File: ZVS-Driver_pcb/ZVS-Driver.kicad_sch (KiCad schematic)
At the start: 29 parts, among them J1 Screw_Terminal_01x02, Q1 IRF540N, Q2 IRF540N, Q3 IRF540N, Q4 IRF540N, Q5 IRF540N, U1 LM317_TO-220

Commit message: new after presntation 15/3
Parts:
- removed C3, C4, C5, C6: C, symbol Device:C
- removed D2: D_Schottky, symbol Device:D_Schottky
- removed D5: D_Zener, symbol Device:D_Zener
- removed L4: L, symbol Device:L
- removed R7, R8: R, Resistor_THT:R_Axial_DIN0207_L6.3mm_D2.5mm_P7.62mm_Horizontal, symbol Device:R
- removed U1: LM317_TO-220, Package_TO_SOT_THT:TO-220-3_Vertical, symbol Regulator_Linear:LM317_TO-220
- added D2: D_Zener, Diode_THT:D_DO-41_SOD81_P12.70mm_Horizontal, symbol Device:D_Zener
- added D6: D_Schottky, Diode_THT:D_DO-41_SOD81_P12.70mm_Horizontal, symbol Device:D_Schottky
- added L2: L, Capacitor_THT:CP_Radial_D10.0mm_P5.00mm, symbol Device:L
- C1: footprint (none) -> Library:C_Rect_L7.2mm_W11.0mm_P5.00mm_FKS2_FKP2_MKS2_MKP2
- C2: footprint (none) -> Library:C_Radial_D10.0mm_H20.0mm_P4.5mm,customia
- D1, D3: footprint (none) -> Diode_THT:D_DO-41_SOD81_P12.70mm_Horizontal
- D4: footprint Diode_SMD:D_SOD-523 -> Diode_THT:D_DO-41_SOD81_P12.70mm_Horizontal
- J1: footprint (none) -> Connector_USB:USB_C_Receptacle_GCT_USB4125-xx-x-0190_6P_TopMnt_Horizontal
- L1: footprint (none) -> customia_LC_tank:C_Rect_L7.2mm_W11.0mm_P5.00mm_FKS2_FKP2_MKS2_MKP2
- L3: footprint (none) -> Capacitor_THT:CP_Radial_D10.0mm_P5.00mm
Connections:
- net GND is gone; now on net 0: J1.1 (Pin_1)
- net 0: now also D2.2 (A)
- net at C1.2, L1.2, L3.2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: now also D6.1 (K)
- net at D4.1 (K), R1.1, R3.1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: now also J1.2 (Pin_2), D6.2 (A), L2.1
- net at C1.1, D1.1 (K), L1.1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: now also L2.2
- net at D1.2 (A), Q2.1 (G), Q5.2 (D)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: now also D2.1 (K)
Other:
- moved on the sheet: J1

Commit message: Allages nikou
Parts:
- L2, L3: footprint Capacitor_THT:CP_Radial_D10.0mm_P5.00mm -> Inductor_THT:L_Radial_D10.0mm_P5.00mm_Fastron_07M
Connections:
- net at D4.1 (K), J1.2 (Pin_2), L2.1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: now also L3.1; no longer D6.2 (A)
- net at D3.1 (K), Q1.1 (G), Q4.2 (D)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: now also D6.2 (A); no longer L3.1
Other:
- moved on the sheet: D6, L3
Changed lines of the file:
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@@
+	(wire
+		(pts
+			(xy 241.3 71.12) (xy 242.57 71.12)
+		)
+		(stroke
+			(width 0)
+			(type default)
+		)
+	)
 	(wire
 		(pts
@@
 	(wire
 		(pts
+			(xy 242.57 81.28) (xy 242.57 71.12)
+		)
+		(stroke
+			(width 0)
+			(type default)
+		)
+	)
+	(wire
+		(pts
 			(xy 215.9 91.44) (xy 213.36 91.44)
 		)
@@
 	(wire
 		(pts
+			(xy 214.63 99.06) (xy 217.17 99.06)
+		)
+		(stroke
+			(width 0.1524)
+			(type solid)
+		)
+	)
+	(wire
+		(pts
 			(xy 190.5 95.25) (xy 190.5 92.71)
 		)
@@
 	(wire
 		(pts
-			(xy 241.3 71.12) (xy 241.3 81.28)
-		)
-		(stroke
-			(width 0.1524)
-			(type solid)
-		)
-	)
-	(wire
-		(pts
 			(xy 212.09 142.24) (xy 212.09 133.35)
 		)
@@
 	(wire
 		(pts
-			(xy 241.3 81.28) (xy 242.57 81.28)
-		)
-		(stroke
-			(width 0.1524)
-			(type solid)
-		)
-	)
-	(wire
-		(pts
 			(xy 212.09 60.96) (xy 212.09 64.77)
 		)
@@
 	(wire
 		(pts
+			(xy 180.34 99.06) (xy 207.01 99.06)
+		)
+		(stroke
+			(width 0)
+			(type default)
+		)
+	)
+	(wire
+		(pts
 			(xy 223.52 85.09) (xy 222.25 85.09)
 		)
@@
 	(wire
 		(pts
-			(xy 208.28 99.06) (xy 180.34 99.06)
-		)
-		(stroke
-			(width 0.1524)
-			(type solid)
-		)
-	)
-	(wire
-		(pts
 			(xy 217.17 64.77) (xy 212.09 64.77)
 		)
@@
 		(pts
 			(xy 204.47 85.09) (xy 204.47 86.36)
-		)
-		(stroke
-			(width 0)
-			(type default)
-		)
-	)
-	(wire
-		(pts
-			(xy 215.9 99.06) (xy 217.17 99.06)
 		)
 		(stroke
@@
 	(symbol
 		(lib_id "Device:D_Schottky")
-		(at 212.09 99.06 180)
+		(at 213.36 109.22 180)
 		(unit 1)
 		(exclude_from_sim no)
@@
 		(fields_autoplaced yes)
 		(property "Reference" "D6"
-			(at 212.4075 92.71 0)
+			(at 213.6775 102.87 0)
 			(effects
 				(font
@@
 		)
 		(property "Value" "D_Schottky"
-			(at 212.4075 95.25 0)
+			(at 213.6775 105.41 0)
 			(effects
 				(font
@@
 		)
 		(property "Footprint" "Diode_THT:D_DO-41_SOD81_P12.70mm_Horizontal"
-			(at 212.09 99.06 0)
+			(at 213.36 109.22 0)
 			(effects
 				(font
@@
 		)
 		(property "Datasheet" "~"
-			(at 212.09 99.06 0)
+			(at 213.36 109.22 0)
 			(effects
 				(font
@@
 		)
 		(property "Description" "Schottky diode"
-			(at 212.09 99.06 0)
+			(at 213.36 109.22 0)
 			(effects
 				(font
@@
 		)
 		(instances
-			(project "ZVS-Driver"
+			(project "ZVS-Driver (1)"
 				(path "/2c7e395d-0d61-44d7-9118-9d4d2f6d8d81"
 					(reference "D6")
@@
 			)
 		)
-		(property "Footprint" "Capacitor_THT:CP_Radial_D10.0mm_P5.00mm"
+		(property "Footprint" "Inductor_THT:L_Radial_D10.0mm_P5.00mm_Fastron_07M"
 			(at 212.09 68.58 0)
 			(effects
@@
 	(symbol
 		(lib_id "Device:L")
-		(at 213.36 109.22 90)
+		(at 210.82 99.06 90)
 		(unit 1)
 		(exclude_from_sim no)
@@
 		(fields_autoplaced yes)
 		(property "Reference" "L3"
-			(at 213.36 104.14 90)
+			(at 210.82 93.98 90)
 			(effects
 				(font
@@
 		)
 		(property "Value" "L"
-			(at 213.36 106.68 90)
-			(effects
-				(font
-					(size 1.27 1.27)
-				)
-			)
-		)
-		(property "Footprint" "Capacitor_THT:CP_Radial_D10.0mm_P5.00mm"
-			(at 213.36 109.22 0)
+			(at 210.82 96.52 90)
+			(effects
+				(font
+					(size 1.27 1.27)
+				)
+			)
+		)
+		(property "Footprint" "Inductor_THT:L_Radial_D10.0mm_P5.00mm_Fastron_07M"
+			(at 210.82 99.06 0)
 			(effects
 				(font
@@
 		)
 		(property "Datasheet" "~"
-			(at 213.36 109.22 0)
+			(at 210.82 99.06 0)
 			(effects
 				(font
@@
 		)
 		(property "Description" "Inductor"
-			(at 213.36 109.22 0)
+			(at 210.82 99.06 0)
 			(effects
 				(font
@@
 		)
 		(instances
-			(project "ZVS-Driver"
+			(project "ZVS-Driver (1)"
 				(path "/2c7e395d-0d61-44d7-9118-9d4d2f6d8d81"
 					(reference "L3")

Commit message: updated heatsinks and screw terminal as an input (havnet put the 4 usb c pins)
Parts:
- added HS1, HS3: Heatsink, Heatsink:Heatsink_Fischer_FK224xx2201_25x8.3mm, symbol Mechanical:Heatsink
- added J2: Screw_Terminal_01x02, TerminalBlock_Phoenix:TerminalBlock_Phoenix_MKDS-1,5-2_1x02_P5.00mm_Horizontal, symbol Connector:Screw_Terminal_01x02
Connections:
- net 0: now also J2.1 (Pin_1)
- net at D4.1 (K), J1.2 (Pin_2), L2.1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: now also J2.2 (Pin_2)

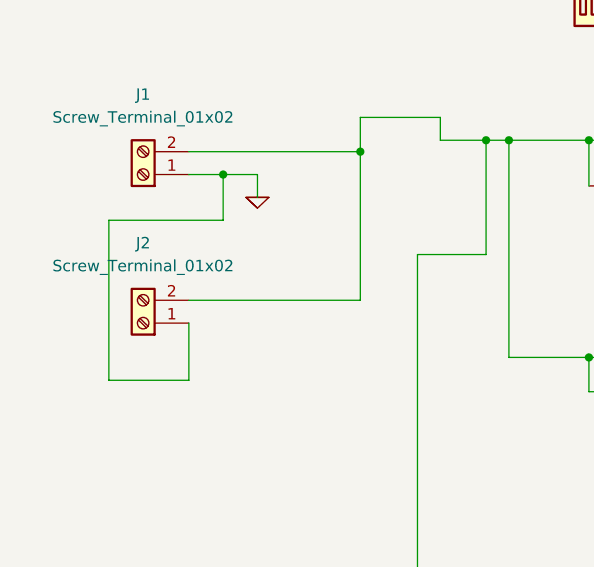
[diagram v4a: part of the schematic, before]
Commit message: usb c eisodos kai routing stis eisodoys
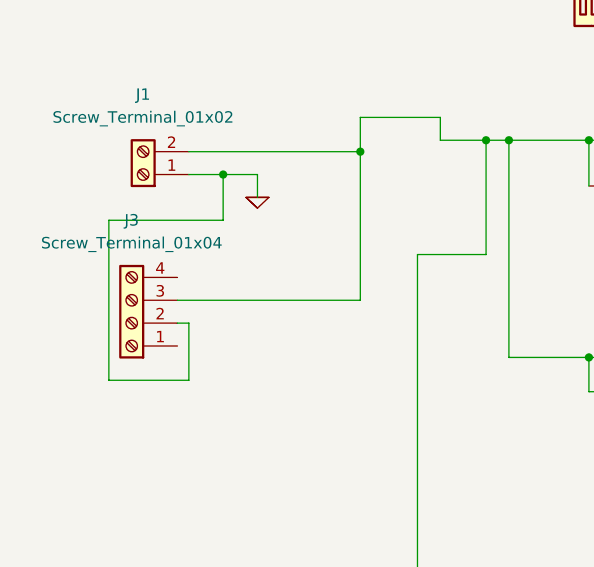
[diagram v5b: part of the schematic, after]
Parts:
- removed J2: Screw_Terminal_01x02, TerminalBlock_Phoenix:TerminalBlock_Phoenix_MKDS-1,5-2_1x02_P5.00mm_Horizontal, symbol Connector:Screw_Terminal_01x02
- added J3: Screw_Terminal_01x04, usb_c_customia:usb_c_customia, symbol Connector:Screw_Terminal_01x04
- J1: footprint Connector_USB:USB_C_Receptacle_GCT_USB4125-xx-x-0190_6P_TopMnt_Horizontal -> TerminalBlock_Phoenix:TerminalBlock_Phoenix_MKDS-1,5-2-5.08_1x02_P5.08mm_Horizontal
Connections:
- net 0: now also J3.2 (Pin_2)
- net at D4.1 (K), J1.2 (Pin_2), L2.1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: now also J3.3 (Pin_3)
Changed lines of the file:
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@@
 	(wire
 		(pts
-			(xy 135.89 88.9) (xy 154.94 88.9)
+			(xy 213.36 74.93) (xy 213.36 78.74)
+		)
+		(stroke
+			(width 0.1524)
+			(type solid)
+		)
+	)
+	(wire
+		(pts
+			(xy 181.61 148.59) (xy 181.61 151.13)
 		)
 		(stroke
@@
 	(wire
 		(pts
-			(xy 213.36 74.93) (xy 213.36 78.74)
-		)
-		(stroke
-			(width 0.1524)
-			(type solid)
-		)
-	)
-	(wire
-		(pts
-			(xy 181.61 148.59) (xy 181.61 151.13)
+			(xy 217.17 64.77) (xy 212.09 64.77)
+		)
+		(stroke
+			(width 0.1524)
+			(type solid)
+		)
+	)
+	(wire
+		(pts
+			(xy 171.45 133.35) (xy 161.29 133.35)
+		)
+		(stroke
+			(width 0.1524)
+			(type solid)
+		)
+	)
+	(wire
+		(pts
+			(xy 233.68 99.06) (xy 241.3 99.06)
+		)
+		(stroke
+			(width 0.1524)
+			(type solid)
+		)
+	)
+	(wire
+		(pts
+			(xy 171.45 124.46) (xy 171.45 120.65)
+		)
+		(stroke
+			(width 0.1524)
+			(type solid)
+		)
+	)
+	(wire
+		(pts
+			(xy 217.17 99.06) (xy 233.68 99.06)
+		)
+		(stroke
+			(width 0.1524)
+			(type solid)
+		)
+	)
+	(wire
+		(pts
+			(xy 242.57 88.9) (xy 242.57 99.06)
 		)
 		(stroke
@@
 	(wire
 		(pts
-			(xy 217.17 64.77) (xy 212.09 64.77)
-		)
-		(stroke
-			(width 0.1524)
-			(type solid)
-		)
-	)
-	(wire
-		(pts
-			(xy 171.45 133.35) (xy 161.29 133.35)
-		)
-		(stroke
-			(width 0.1524)
-			(type solid)
-		)
-	)
-	(wire
-		(pts
-			(xy 233.68 99.06) (xy 241.3 99.06)
-		)
-		(stroke
-			(width 0.1524)
-			(type solid)
-		)
-	)
-	(wire
-		(pts
-			(xy 171.45 124.46) (xy 171.45 120.65)
-		)
-		(stroke
-			(width 0.1524)
-			(type solid)
-		)
-	)
-	(wire
-		(pts
-			(xy 217.17 99.06) (xy 233.68 99.06)
-		)
-		(stroke
-			(width 0.1524)
-			(type solid)
-		)
-	)
-	(wire
-		(pts
-			(xy 242.57 88.9) (xy 242.57 99.06)
+			(xy 161.29 120.65) (xy 161.29 121.92)
 		)
 		(stroke
@@
 	(wire
 		(pts
-			(xy 161.29 120.65) (xy 161.29 121.92)
+			(xy 208.28 68.58) (xy 208.28 71.12)
+		)
+		(stroke
+			(width 0.1524)
+			(type solid)
+		)
+	)
+	(wire
+		(pts
+			(xy 190.5 95.25) (xy 193.04 95.25)
+		)
+		(stroke
+			(width 0.1524)
+			(type solid)
+		)
+	)
+	(wire
+		(pts
+			(xy 219.71 135.89) (xy 219.71 119.38)
+		)
+		(stroke
+			(width 0.1524)
+			(type solid)
+		)
+	)
+	(wire
+		(pts
+			(xy 193.04 85.09) (xy 186.69 85.09)
+		)
+		(stroke
+			(width 0.1524)
+			(type solid)
+		)
+	)
+	(wire
+		(pts
+			(xy 134.62 91.44) (xy 135.89 91.44)
 		)
 		(stroke
@@
 	(wire
 		(pts
-			(xy 208.28 68.58) (xy 208.28 71.12)
-		)
-		(stroke
-			(width 0.1524)
-			(type solid)
-		)
-	)
-	(wire
-		(pts
-			(xy 190.5 95.25) (xy 193.04 95.25)
-		)
-		(stroke
-			(width 0.1524)
-			(type solid)
-		)
-	)
-	(wire
-		(pts
-			(xy 219.71 135.89) (xy 219.71 119.38)
-		)
-		(stroke
-			(width 0.1524)
-			(type solid)
-		)
-	)
-	(wire
-		(pts
-			(xy 193.04 85.09) (xy 186.69 85.09)
-		)
-		(stroke
-			(width 0.1524)
-			(type solid)
-		)
-	)
-	(wire
-		(pts
 			(xy 161.29 139.7) (xy 161.29 140.97)
 		)
@@
 			(width 0.1524)
 			(type solid)
+		)
+	)
+	(wire
+		(pts
+			(xy 134.62 88.9) (xy 154.94 88.9)
+		)
+		(stroke
+			(width 0)
+			(type default)
 		)
 	)
@@
 	)
 	(symbol
+		(lib_id "Connector:Screw_Terminal_01x04")
+		(at 129.54 91.44 180)
+		(unit 1)
+		(exclude_from_sim no)
+		(in_bom yes)
+		(on_board yes)
+		(dnp no)
+		(fields_autoplaced yes)
+		(property "Reference" "J3"
+			(at 129.54 80.01 0)
+			(effects
+				(font
+					(size 1.27 1.27)
+				)
+			)
+		)
+		(property "Value" "Screw_Terminal_01x04"
+			(at 129.54 82.55 0)
+			(effects
+				(font
+					(size 1.27 1.27)
+				)
+			)
+		)
+		(property "Footprint" "usb_c_customia:usb_c_customia"
+			(at 129.54 91.44 0)
+			(effects
+				(font
+					(size 1.27 1.27)
+				)
+				(hide yes)
+			)
+		)
+		(property "Datasheet" "~"
+			(at 129.54 91.44 0)
+			(effects
+				(font
+					(size 1.27 1.27)
+				)
+				(hide yes)
+			)
+		)
+		(property "Description" "Generic screw terminal, single row, 01x04, script generated (kicad-library-utils/schlib/autogen/connector/)"
+			(at 129.54 91.44 0)
+			(effects
+				(font
+					(size 1.27 1.27)
+				)
+				(hide yes)
+			)
+		)
+		(pin "4"
+		)
+		(pin "3"
+		)
+		(pin "2"
+		)
+		(pin "1"
+		)
+		(instances
+			(project ""
+				(path "/2c7e395d-0d61-44d7-9118-9d4d2f6d8d81"
+					(reference "J3")
+					(unit 1)
+				)
+			)
+		)
+	)
+	(symbol
 		(lib_id "ltspice:GND")
 		(at 161.29 149.86 0)
@@
 	)
 	(symbol
-		(lib_id "Connector:Screw_Terminal_01x02")
-		(at 130.81 91.44 180)
-		(unit 1)
-		(exclude_from_sim no)
-		(in_bom yes)
-		(on_board yes)
-		(dnp no)
-		(fields_autoplaced yes)
-		(property "Reference" "J2"
-			(at 130.81 82.55 0)
-			(effects
-				(font
-					(size 1.27 1.27)
-				)
-			)
-		)
-		(property "Value" "Screw_Terminal_01x02"
-			(at 130.81 85.09 0)
-			(effects
-				(font
-					(size 1.27 1.27)
-				)
-			)
-		)
-		(property "Footprint" "TerminalBlock_Phoenix:TerminalBlock_Phoenix_MKDS-1,5-2_1x02_P5.00mm_Horizontal"
-			(at 130.81 91.44 0)
-			(effects
-				(font
-					(size 1.27 1.27)
-				)
-				(hide yes)
-			)
-		)
-		(property "Datasheet" "~"
-			(at 130.81 91.44 0)
-			(effects
-				(font
-					(size 1.27 1.27)
-				)
-				(hide yes)
-			)
-		)
-		(property "Description" "Generic screw terminal, single row, 01x02, script generated (kicad-library-utils/schlib/autogen/connector/)"
-			(at 130.81 91.44 0)
-			(effects
-				(font
-					(size 1.27 1.27)
-				)
-				(hide yes)
-			)
-		)
-		(pin "2"
-		)
-		(pin "1"
-		)
-		(instances
-			(project "ZVS-Driver"
-				(path "/2c7e395d-0d61-44d7-9118-9d4d2f6d8d81"
-					(reference "J2")
-					(unit 1)
-				)
-			)
-		)
-	)
-	(symbol
 		(lib_id "Device:D_Schottky")
 		(at 213.36 109.22 180)
@@
 			)
 		)
-		(property "Footprint" "Connector_USB:USB_C_Receptacle_GCT_USB4125-xx-x-0190_6P_TopMnt_Horizontal"
+		(property "Footprint" "TerminalBlock_Phoenix:TerminalBlock_Phoenix_MKDS-1,5-2-5.08_1x02_P5.08mm_Horizontal"
 			(at 130.81 74.93 0)
 			(effects

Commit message: Spiti alex
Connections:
- net 0: now also J3.1 (Pin_1); no longer J3.2 (Pin_2)
- net at D4.1 (K), J1.2 (Pin_2), L2.1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: now also J3.4 (Pin_4); no longer J3.3 (Pin_3)
- net at C1.2, D6.1 (K), L3.2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: now also L1.1; no longer L1.2
- net at C1.1, D1.1 (K), L2.2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: now also L1.2; no longer L1.1
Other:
- moved on the sheet: L1
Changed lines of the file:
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@@
+	)
+	(junction
+		(at 180.34 71.12)
+		(diameter 0)
+		(color 0 0 0 0)
+	)
+	(junction
+		(at 222.25 85.09)
+		(diameter 0)
+		(color 0 0 0 0)
+	)
+	(junction
+		(at 198.12 74.93)
+		(diameter 0)
+		(color 0 0 0 0)
+	)
+	(junction
+		(at 204.47 85.09)
+		(diameter 0)
+		(color 0 0 0 0)
+	)
+	(junction
+		(at 161.29 133.35)
+		(diameter 0)
+		(color 0 0 0 0)
+	)
+	(junction
+		(at 180.34 95.25)
+		(diameter 0)
+		(color 0 0 0 0)
+	)
+	(junction
+		(at 205.74 95.25)
+		(diameter 0)
+		(color 0 0 0 0)
+	)
+	(junction
+		(at 217.17 71.12)
+		(diameter 0)
+		(color 0 0 0 0)
+	)
+	(junction
+		(at 233.68 71.12)
+		(diameter 0)
+		(color 0 0 0 0)
+	)
+	(junction
+		(at 193.04 95.25)
+		(diameter 0)
+		(color 0 0 0 0)
+	)
+	(junction
+		(at 171.45 120.65)
+		(diameter 0)
+		(color 0 0 0 0)
+	)
+	(junction
+		(at 204.47 95.25)
+		(diameter 0)
+		(color 0 0 0 0)
+	)
+	(junction
+		(at 168.91 71.12)
+		(diameter 0)
+		(color 0 0 0 0)
+	)
+	(junction
+		(at 200.66 95.25)
+		(diameter 0)
+		(color 0 0 0 0)
+	)
+	(junction
+		(at 199.39 74.93)
+		(diameter 0)
+		(color 0 0 0 0)
+	)
+	(junction
+		(at 181.61 135.89)
+		(diameter 0)
+		(color 0 0 0 0)
+	)
+	(junction
+		(at 193.04 135.89)
+		(diameter 0)
+		(color 0 0 0 0)
+	)
+	(junction
+		(at 171.45 71.12)
+		(diameter 0)
+		(color 0 0 0 0)
+	)
+	(junction
+		(at 161.29 120.65)
+		(diameter 0)
+		(color 0 0 0 0)
+	)
+	(junction
+		(at 217.17 99.06)
+		(diameter 0)
+		(color 0 0 0 0)
+	)
+	(junction
+		(at 161.29 139.7)
+		(diameter 0)
+		(color 0 0 0 0)
+	)
+	(junction
+		(at 233.68 99.06)
+		(diameter 0)
+		(color 0 0 0 0)
+	)
+	(junction
+		(at 139.7 74.93)
+		(diameter 0)
+		(color 0 0 0 0)
 	)
 	(junction
@@
 		(color 0 0 0 0)
 	)
-	(junction
-		(at 180.34 71.12)
-		(diameter 0)
-		(color 0 0 0 0)
-	)
-	(junction
-		(at 222.25 85.09)
-		(diameter 0)
-		(color 0 0 0 0)
-	)
-	(junction
-		(at 198.12 74.93)
-		(diameter 0)
-		(color 0 0 0 0)
-	)
-	(junction
-		(at 204.47 85.09)
-		(diameter 0)
-		(color 0 0 0 0)
-	)
-	(junction
-		(at 161.29 133.35)
-		(diameter 0)
-		(color 0 0 0 0)
-	)
-	(junction
-		(at 180.34 95.25)
-		(diameter 0)
-		(color 0 0 0 0)
-	)
-	(junction
-		(at 205.74 95.25)
-		(diameter 0)
-		(color 0 0 0 0)
-	)
-	(junction
-		(at 217.17 71.12)
-		(diameter 0)
-		(color 0 0 0 0)
-	)
-	(junction
-		(at 233.68 71.12)
-		(diameter 0)
-		(color 0 0 0 0)
-	)
-	(junction
-		(at 193.04 95.25)
-		(diameter 0)
-		(color 0 0 0 0)
-	)
-	(junction
-		(at 171.45 120.65)
-		(diameter 0)
-		(color 0 0 0 0)
-	)
-	(junction
-		(at 204.47 95.25)
-		(diameter 0)
-		(color 0 0 0 0)
-	)
-	(junction
-		(at 168.91 71.12)
-		(diameter 0)
-		(color 0 0 0 0)
-	)
-	(junction
-		(at 200.66 95.25)
-		(diameter 0)
-		(color 0 0 0 0)
-	)
-	(junction
-		(at 199.39 74.93)
-		(diameter 0)
-		(color 0 0 0 0)
-	)
-	(junction
-		(at 181.61 135.89)
-		(diameter 0)
-		(color 0 0 0 0)
-	)
-	(junction
-		(at 193.04 135.89)
-		(diameter 0)
-		(color 0 0 0 0)
-	)
-	(junction
-		(at 171.45 71.12)
-		(diameter 0)
-		(color 0 0 0 0)
-	)
-	(junction
-		(at 161.29 120.65)
-		(diameter 0)
-		(color 0 0 0 0)
-	)
-	(junction
-		(at 217.17 99.06)
-		(diameter 0)
-		(color 0 0 0 0)
-	)
-	(junction
-		(at 161.29 139.7)
-		(diameter 0)
-		(color 0 0 0 0)
-	)
-	(junction
-		(at 233.68 99.06)
-		(diameter 0)
-		(color 0 0 0 0)
-	)
-	(junction
-		(at 139.7 74.93)
-		(diameter 0)
-		(color 0 0 0 0)
-	)
 	(wire
 		(pts
@@
 	(wire
 		(pts
+			(xy 135.89 97.79) (xy 135.89 93.98)
+		)
+		(stroke
+			(width 0)
+			(type default)
+		)
+	)
+	(wire
+		(pts
 			(xy 193.04 135.89) (xy 193.04 133.35)
 		)
@@
 	(wire
 		(pts
-			(xy 134.62 91.44) (xy 135.89 91.44)
-		)
-		(stroke
-			(width 0)
-			(type default)
-		)
-	)
-	(wire
-		(pts
 			(xy 161.29 139.7) (xy 161.29 140.97)
 		)
@@
 	(wire
 		(pts
-			(xy 135.89 91.44) (xy 135.89 97.79)
-		)
-		(stroke
-			(width 0)
-			(type default)
-		)
-	)
-	(wire
-		(pts
 			(xy 204.47 74.93) (xy 204.47 76.2)
 		)
@@
 	(wire
 		(pts
-			(xy 154.94 88.9) (xy 154.94 72.39)
-		)
-		(stroke
-			(width 0)
-			(type default)
-		)
-	)
-	(wire
-		(pts
 			(xy 171.45 95.25) (xy 171.45 71.12)
 		)
@@
 	(wire
 		(pts
+			(xy 134.62 93.98) (xy 135.89 93.98)
+		)
+		(stroke
+			(width 0)
+			(type default)
+		)
+	)
+	(wire
+		(pts
 			(xy 204.47 85.09) (xy 222.25 85.09)
 		)
@@
 	(wire
 		(pts
+			(xy 154.94 72.39) (xy 154.94 86.36)
+		)
+		(stroke
+			(width 0)
+			(type default)
+		)
+	)
+	(wire
+		(pts
 			(xy 219.71 137.16) (xy 219.71 135.89)
 		)
@@
 	(wire
 		(pts
-			(xy 134.62 88.9) (xy 154.94 88.9)
-		)
-		(stroke
-			(width 0)
-			(type default)
-		)
-	)
-	(wire
-		(pts
 			(xy 215.9 142.24) (xy 212.09 142.24)
 		)
@@
 			(width 0.1524)
 			(type solid)
+		)
+	)
+	(wire
+		(pts
+			(xy 134.62 86.36) (xy 154.94 86.36)
+		)
+		(stroke
+			(width 0)
+			(type default)
 		)
 	)
@@
 	(symbol
 		(lib_id "Device:L")
-		(at 242.57 85.09 0)
+		(at 242.57 85.09 180)
 		(unit 1)
 		(exclude_from_sim no)
@@
 					(size 1.27 1.27)
 				)
-				(justify left)
+				(justify right)
 			)
 		)
@@
 					(size 1.27 1.27)
 				)
-				(justify left)
-			)
-		)
+				(justify right)
+			)
+		)
